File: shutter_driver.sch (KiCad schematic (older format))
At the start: 41 parts, among them J1 SHUTTER, J2 POWER, J3 I/O, J4 FRONT, Q1 2N3904, Q2 FQP30N06L-ND, Q3 2N3904, Q4 2N3904, Q5 Q_PMOS_GDS, SW1 SW_DPDT_x2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

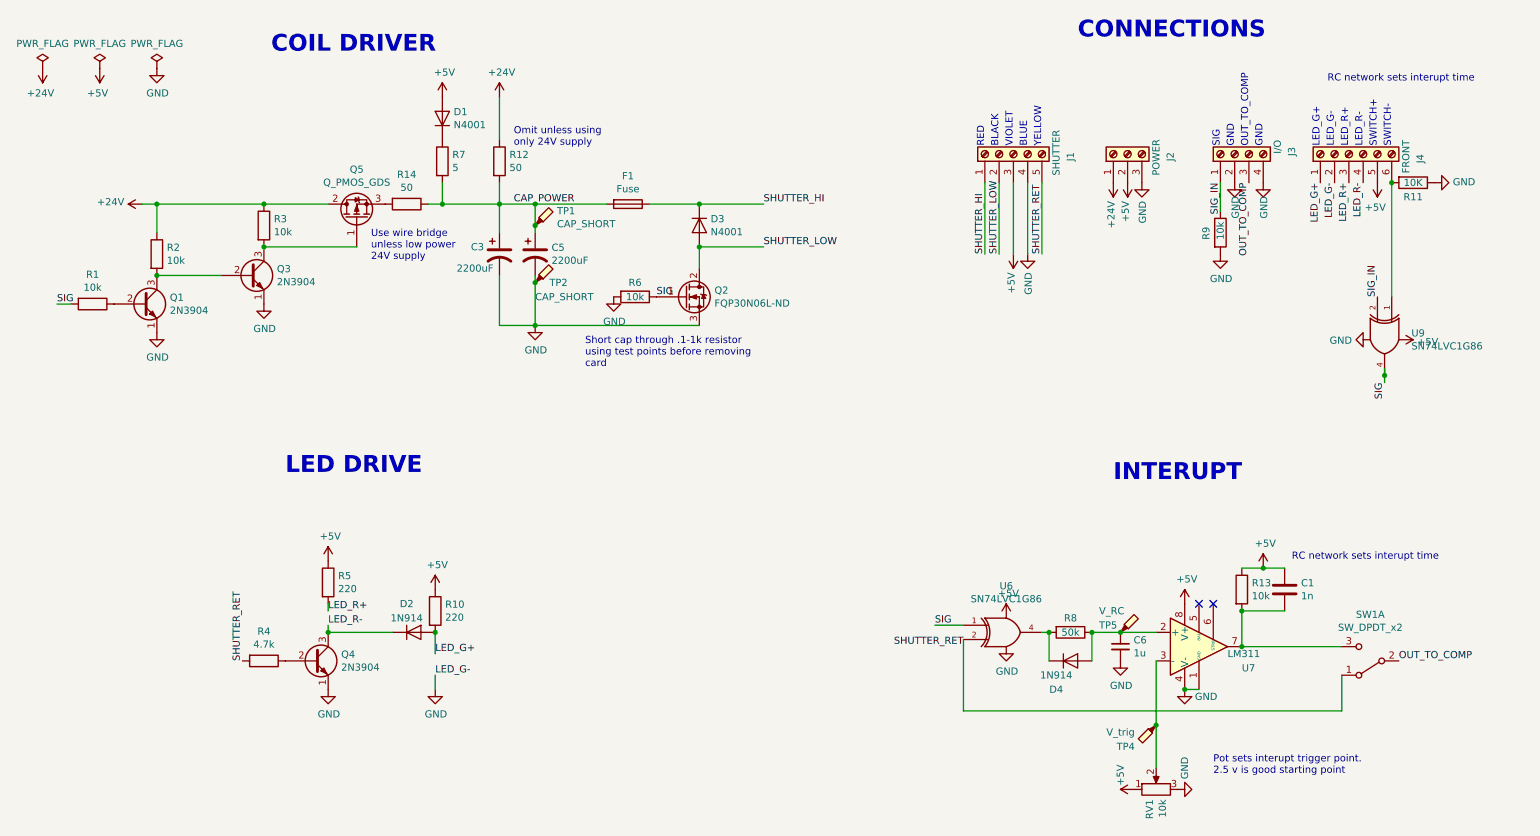
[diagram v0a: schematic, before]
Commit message: simplified schamatic for poster.
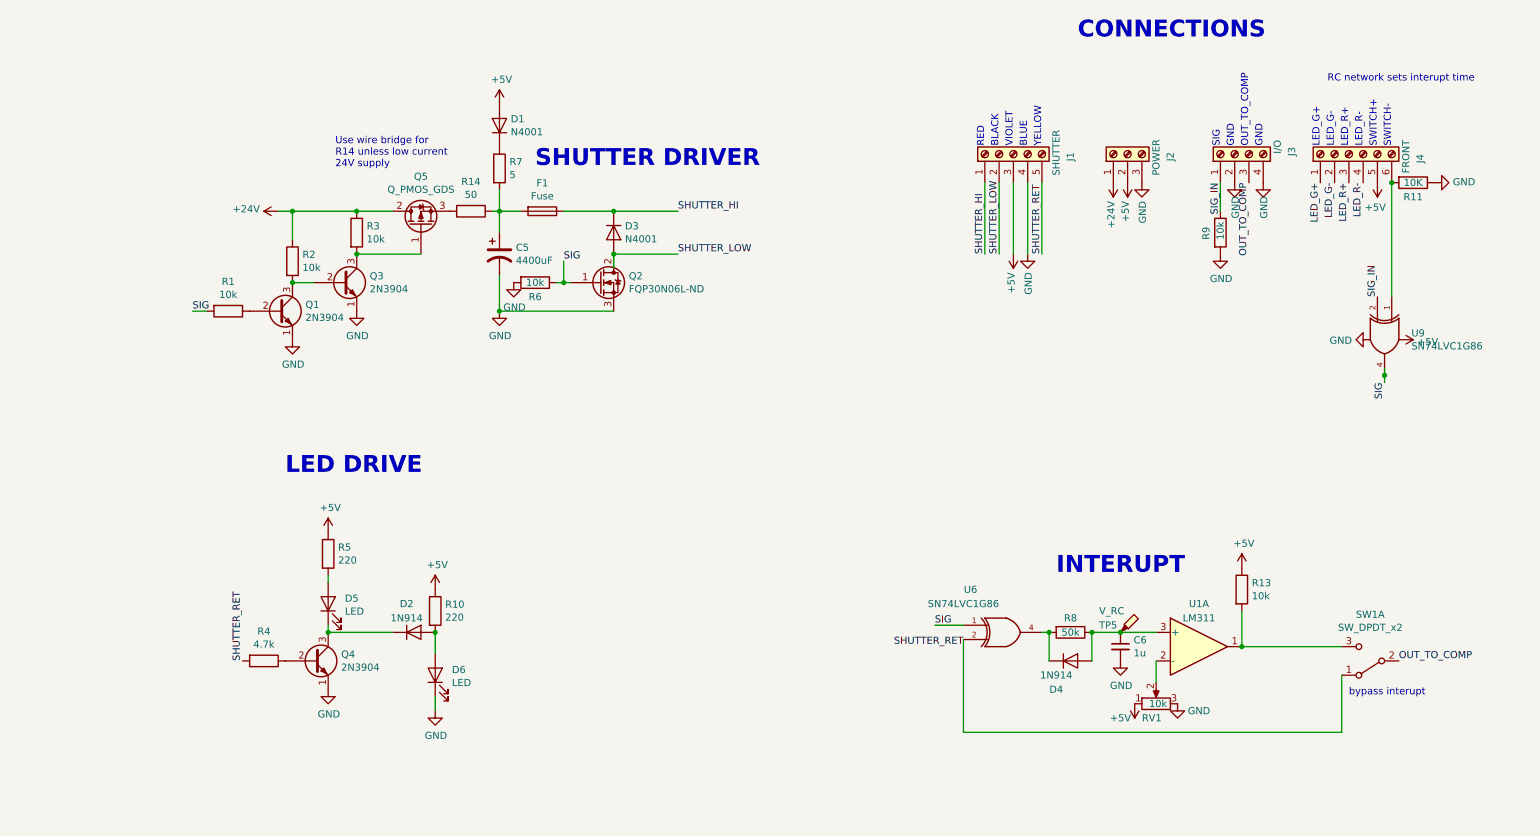
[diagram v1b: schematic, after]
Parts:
- removed C1: 1n, Capacitors_THT:C_Disc_D5.0mm_W2.5mm_P5.00mm, symbol Device:C
- removed C3: 2200uF, Capacitors_THT:CP_Radial_D16.0mm_P7.50mm, symbol Device:CP1
- removed R12: 50, Resistors_THT:R_Axial_Power_L25.0mm_W9.0mm_P30.48mm, symbol Device:R
- removed TP1, TP2: CAP_SHORT, Measurement_Points:Measurement_Point_Round-SMD-Pad_Small, symbol Connector:TestPoint_Probe
- removed TP4: V_trig, Measurement_Points:Measurement_Point_Round-SMD-Pad_Small, symbol Connector:TestPoint_Probe
- removed U7: LM311, Housings_DIP:DIP-8_W7.62mm_LongPads, symbol Comparator:LM311
- added D5, D6: LED, symbol Device:LED
- added U1: LM311, symbol Amplifier_Audio:TDA1308
- C5: value 2200uF -> 4400uF
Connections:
- net labels removed: CAP_POWER
- wire segments 57 -> 46
- no-connect marks 2 -> 0
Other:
- note added: "SHUTTER DRIVER\n"
- note added: "Use wire bridge for\nR14 unless low current\n24V supply"
- note added: "bypass interupt"
- note removed: "COIL DRIVER\n"
- note removed: "Omit unless using \nonly 24V supply"
- note removed: "Pot sets interupt trigger point. \n2.5 v is good starting point"
- note removed: "Short cap through .1-1k resistor\nusing test points before removing\ncard"
- note removed: "Use wire bridge\nunless low power\n24V supply"
- moved on the sheet: C5, D1, D3, F1, Q1, Q2, Q3, Q5, R1, R14, R2, R3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

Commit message: spelling interrupt
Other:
- note added: "INTERRUPT"
- note removed: "INTERUPT"
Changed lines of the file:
@@
 SHUTTER DRIVER\n
 Text Notes 7950 4550 0    118  ~ 24
-INTERUPT
+INTERRUPT
 Text Notes 8100 800  0    118  ~ 24
 CONNECTIONS
